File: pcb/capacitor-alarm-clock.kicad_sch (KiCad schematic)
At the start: 13 parts

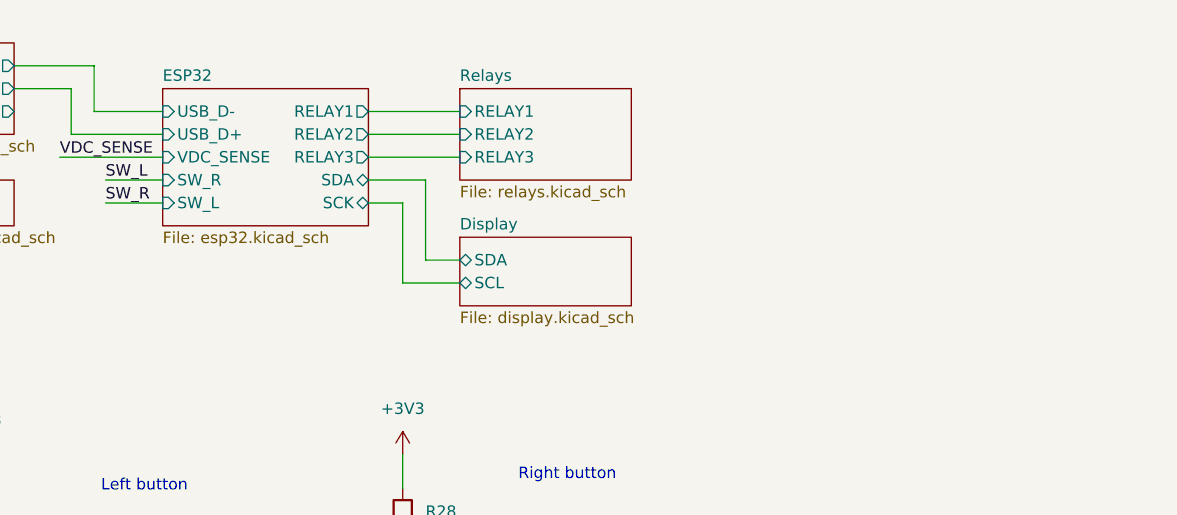
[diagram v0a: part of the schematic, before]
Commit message: Connected reset pin to gpio2
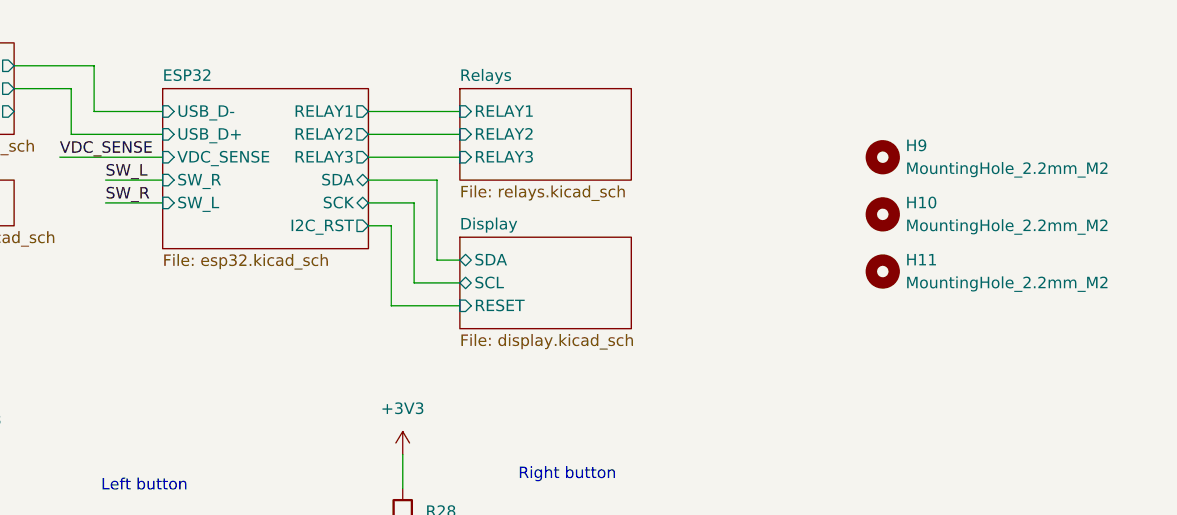
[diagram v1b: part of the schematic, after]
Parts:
- added H10, H11, H9: MountingHole_2.2mm_M2, MountingHole:MountingHole_2.2mm_M2, symbol Mechanical:MountingHole
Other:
- sheet Display ports: added RESET; removed none
- sheet ESP32 ports: added I2C_RST; removed none

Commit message: Upgrade kicad version to 10, add krita capacitor image
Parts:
- H1, SW2, SW4, U3: value ~ -> (none)

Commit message: Add JLC carts and BOM
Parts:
- C14, C15: Manufacturer Part (none) -> CL10B105KA8NNNC; Supplier (none) -> LCSC; Supplier Part C15849 -> C29936; Supplier Part URL (none) -> https://www.lcsc.com/product-detail/C29936.html
- C3, C4: Manufacturer Part (none) -> CL10A106KP8NNNC; Supplier (none) -> LCSC; Supplier Part URL (none) -> https://www.lcsc.com/product-detail/C19702.html
- D1: Supplier Part URL (none) -> https://www.lcsc.com/product-detail/C173413.html
- H1: now left out of the parts list
- R27, R28, R6: Manufacturer Part (none) -> RC0603FR-0710KL; Supplier (none) -> LCSC; Supplier Part URL (none) -> https://www.lcsc.com/product-detail/C98220.html
- R7: Manufacturer Part (none) -> RC0603FR-0762KL; Supplier (none) -> LCSC; Supplier Part URL (none) -> https://www.lcsc.com/product-detail/C137694.html
- SW2, SW4: Supplier Part URL (none) -> https://www.lcsc.com/product-detail/C557599.html
- U3: Supplier Part URL (none) -> https://www.lcsc.com/product-detail/C7434186.html

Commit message: Update 10u capacitor to 25v rated one
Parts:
- C3, C4: Manufacturer Part CL10A106KP8NNNC -> CL10A106MA8NRNC; Supplier Part C19702 -> C96446; Supplier Part URL https://www.lcsc.com/product-detail/C19702.html -> https://www.lcsc.com/product-detail/C96446.html
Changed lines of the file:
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@@
 			)
 		)
-		(property "Supplier Part" "C19702"
+		(property "Supplier Part" "C96446"
 			(at 77.47 143.51 0)
 			(hide yes)
@@
 			)
 		)
-		(property "Manufacturer Part" "CL10A106KP8NNNC"
+		(property "Manufacturer Part" "CL10A106MA8NRNC"
 			(at 77.47 143.51 0)
 			(hide yes)
@@
 			)
 		)
-		(property "Supplier Part URL" "https://www.lcsc.com/product-detail/C19702.html"
+		(property "Supplier Part URL" "https://www.lcsc.com/product-detail/C96446.html"
 			(at 77.47 143.51 0)
 			(hide yes)
@@
 			)
 		)
-		(property "Supplier Part" "C19702"
+		(property "Supplier Part" "C96446"
 			(at 115.57 143.51 0)
 			(hide yes)
@@
 			)
 		)
-		(property "Manufacturer Part" "CL10A106KP8NNNC"
+		(property "Manufacturer Part" "CL10A106MA8NRNC"
 			(at 115.57 143.51 0)
 			(hide yes)
@@
 			)
 		)
-		(property "Supplier Part URL" "https://www.lcsc.com/product-detail/C19702.html"
+		(property "Supplier Part URL" "https://www.lcsc.com/product-detail/C96446.html"
 			(at 115.57 143.51 0)
 			(hide yes)

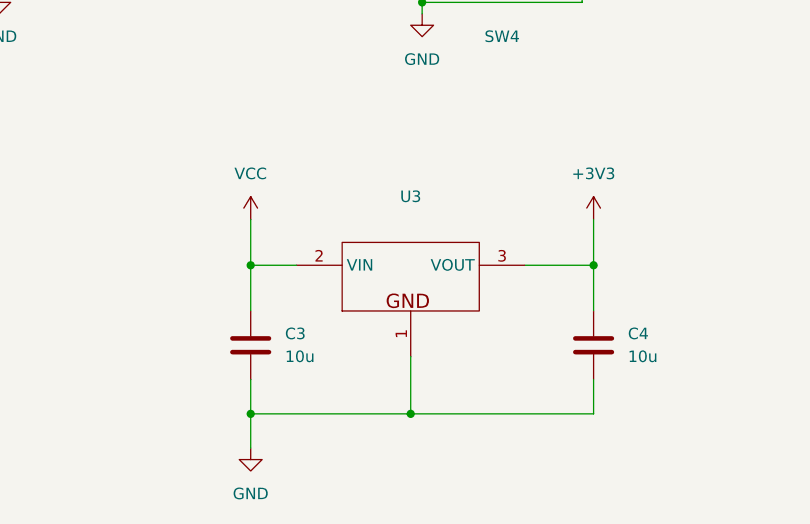
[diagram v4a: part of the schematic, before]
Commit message: Improve voltage regulator circuit so it doesn't keep browning out
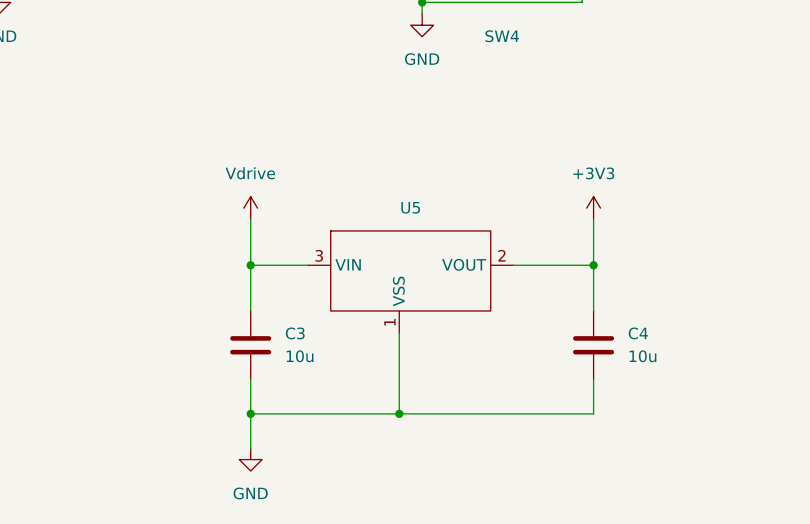
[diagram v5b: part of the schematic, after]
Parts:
- removed U3: (no value), EasyEDA_Lib:SOT-89-3_L4.5-W2.5-P1.50-LS4.2-BR, symbol EasyEDA_Lib:HT7333-1-MS_C7434186
- added U5: (no value), EasyEDA_Lib:SOT-223-3_L6.5-W3.4-P2.30-LS7.0-BR-1, symbol EasyEDA_Lib:SSP7903P33FR
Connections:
- net +3V3: now also U5.2 (VOUT)
- net GND: now also U5.1 (VSS)
- net VCC: no longer C3.1
- new net Vdrive: C3.1, U5.3 (VIN)
